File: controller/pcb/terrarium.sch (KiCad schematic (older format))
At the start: 61 parts, among them Q1 S8050, Q2 S8050, Q3 S8050, Q4 S8050, SW1 RESET, SW3 RTC BATTERY, U1 ESP32-WROOM-32, U2 DS3231M, U3 LM1117-3.3

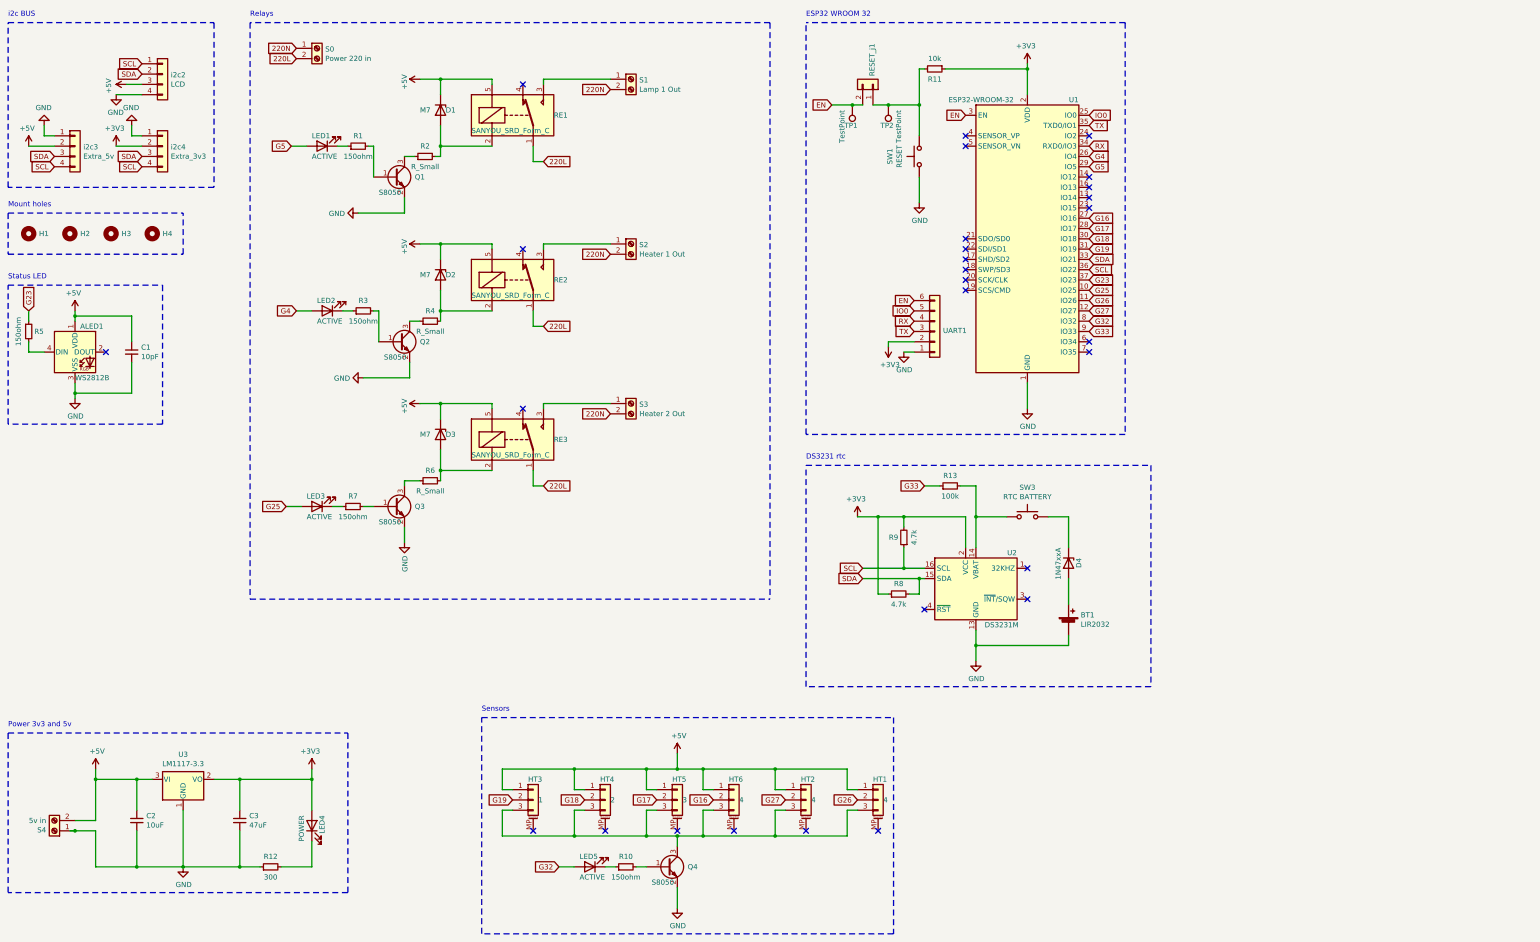
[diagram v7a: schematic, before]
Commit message: move status led from relay circuit
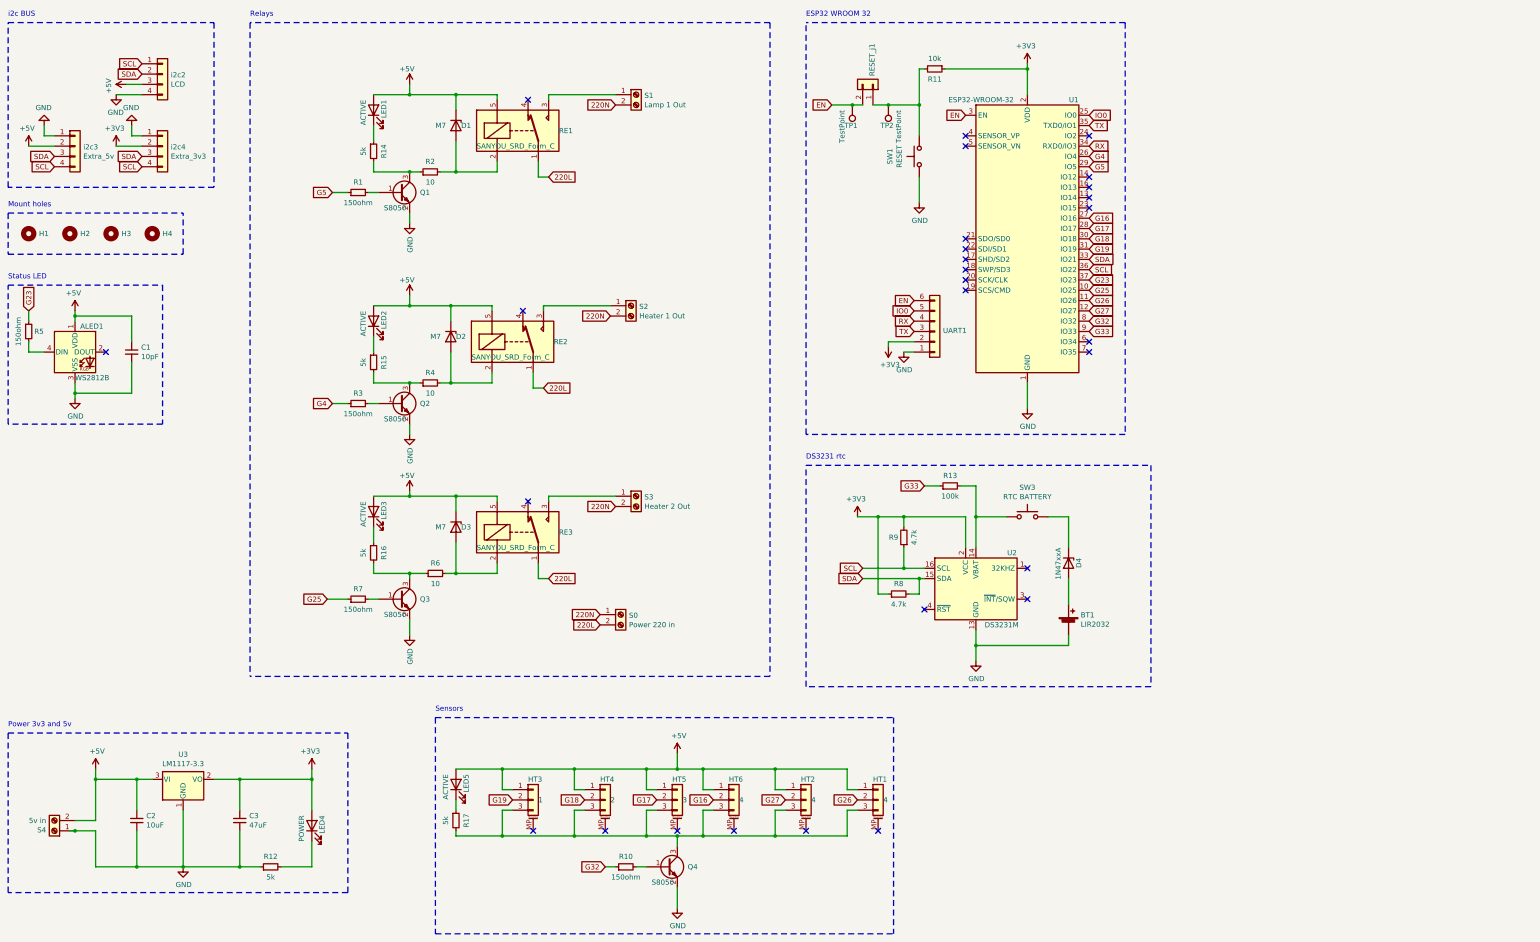
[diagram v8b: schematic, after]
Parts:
- added R14, R15, R16, R17: 5k, Resistor_SMD:R_1206_3216Metric, symbol Device:R_Small
- R12: value 300 -> 5k
- R2, R4, R6: value R_Small -> 10
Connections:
- net +5V: now also LED1.2 (A), LED2.2 (A), LED3.2 (A), LED5.2 (A)
- net G25: now also R7.1; no longer LED3.2 (A)
- net G32: now also R10.1; no longer LED5.2 (A)
- net G4: now also R3.1; no longer LED2.2 (A)
- net G5: now also R1.1; no longer LED1.2 (A)
- net at HT1.3 (Pin_3), HT2.3 (Pin_3), HT3.3 (Pin_3)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: now also R17.2
- net at Q2.3 (C), R4.1: now also R15.2
- net at Q1.3 (C), R2.1: now also R14.2
- net at LED1.1 (K): now also R14.1; no longer R1.1
- net at LED2.1 (K): now also R15.1; no longer R3.1
- net at Q3.3 (C), R6.1: now also R16.2
- net at LED3.1 (K): now also R16.1; no longer R7.1
- net at LED5.1 (K): now also R17.1; no longer R10.1
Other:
- moved on the sheet: D1, D2, D3, LED1, LED2, LED3, LED5, Q1, Q2, Q3, R1, R2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
